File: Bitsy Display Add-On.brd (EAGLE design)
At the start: 35.6 x 17.8 mm, 13 parts, among them IC1 APX803, SW1 KMR2

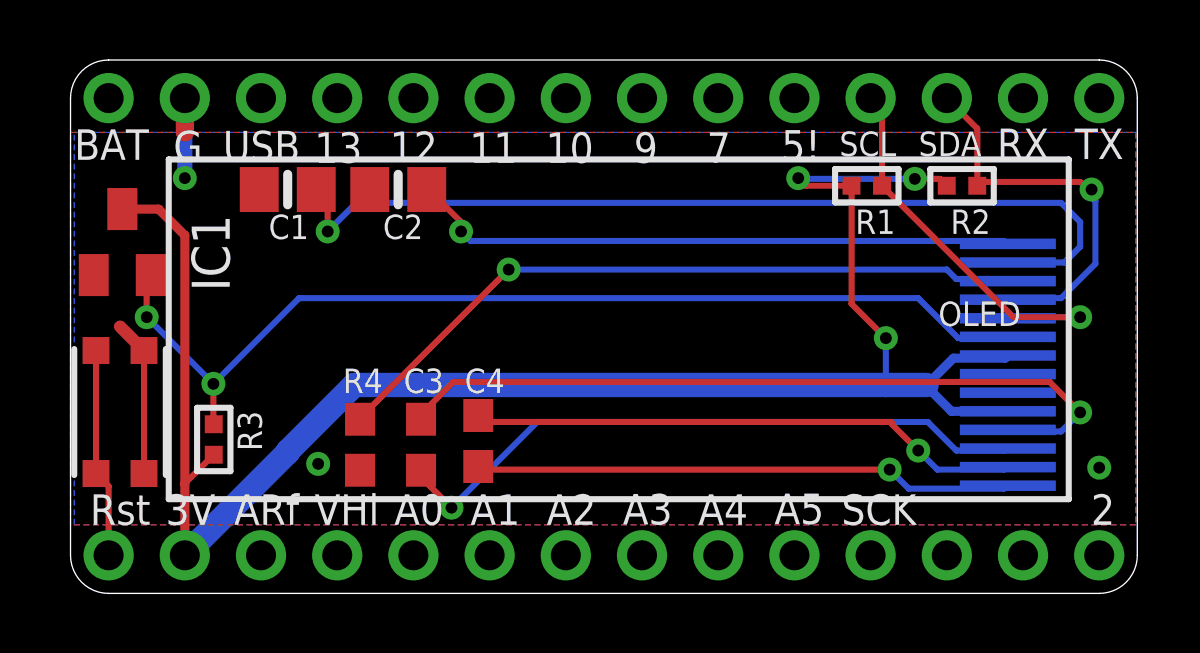
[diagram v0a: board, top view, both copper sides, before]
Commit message: PCB Redisgned
Resistors and Capacitors on bottom of board
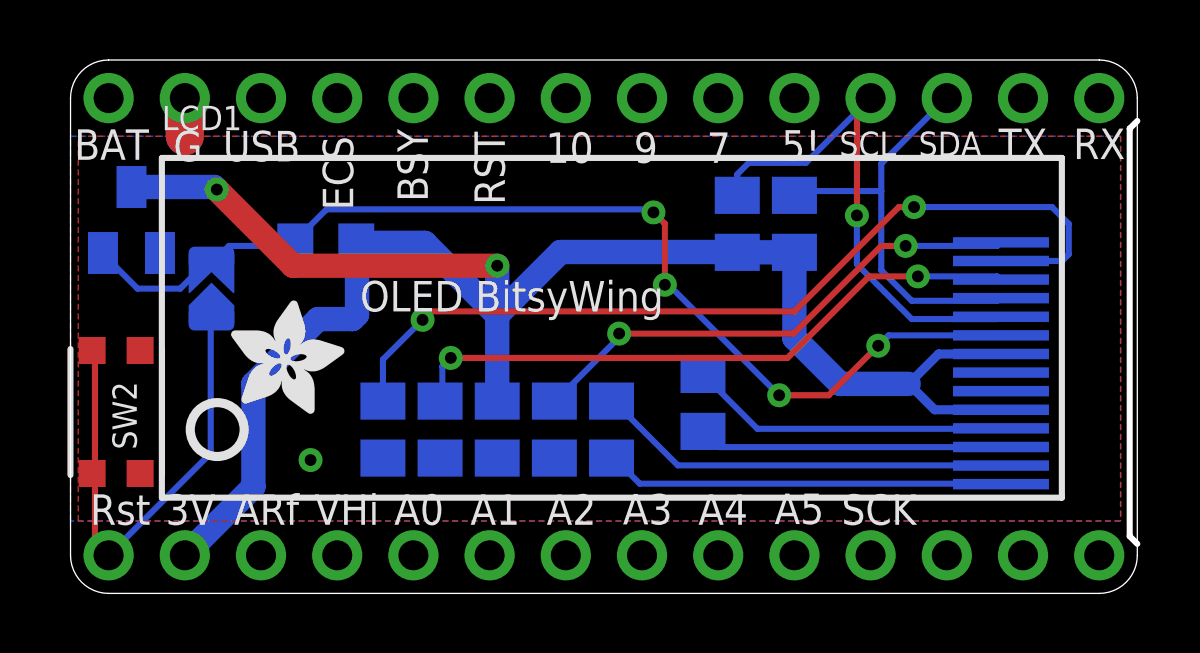
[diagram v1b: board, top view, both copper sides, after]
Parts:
- removed C3: 1uF, microbuilder:0603-NO
- removed IC1: APX803, adafruit:SOT23
- removed JP1: (no value), microbuilder:1X14_ROUND70
- removed OLED: OLED 128x32, microbuilder:UG-2832HSWEG02_WRAPUNDER
- removed R1: 2K, microbuilder:_0402
- removed SW1: KMR2, microbuilder:BTN_KMR2_4.6X2.8
- added C5, C6: 10uF, microbuilder:0805-NO
- added IC5: APX803, adafruit:SOT23
- added JP4: (no value), microbuilder:1X14_ROUND70
- added LCD1: OLED 128x32, microbuilder:UG-2832HSWEG02_WRAPUNDER
- added R7: 2.2K, microbuilder:0805-NO
- added SJ1: (no value), microbuilder:SOLDERJUMPER_ARROW_NOPASTE
- added SW2: KMR2, microbuilder:BTN_KMR2_4.6X2.8
- added U$6: (no value), microbuilder:PCBFEAT-REV-040
- added U$62: (no value), microbuilder:ADAFRUIT_3.5MM
- C1, C2: value 10uF -> 1uF
- C4: value 1uF -> 10uF; device microbuilder:0603-NO -> microbuilder:0805-NO
- R2: value 2K -> 10K; device microbuilder:_0402 -> microbuilder:_0805MP
- R3: value 10K -> 390K; device microbuilder:_0402 -> microbuilder:0805-NO
- R4: value 390K -> 2.2K; device microbuilder:0603-NO -> microbuilder:0805-NO
- moved R2 21.3 mm to (8.51, 11.7), flipped to the bottom
- moved R4 16.2 mm to (24.1, 12.3), flipped to the bottom, turned to 270 degrees
- moved JP2 15.2 mm to (17.8, 16.5), turned to 0 degrees
- moved C1 13.4 mm to (18.0, 5.46), flipped to the bottom, turned to 270 degrees
- moved C2 12.4 mm to (21.1, 6.35), flipped to the bottom, turned to 270 degrees
- moved R3 7.55 mm to (12.3, 5.46), flipped to the bottom, turned to 90 degrees
- moved C4 0.74 mm to (14.2, 5.46), flipped to the bottom, turned to 90 degrees
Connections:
- removed net VCC: C2.2, OLED.14
- removed net VCOMH: C1.2, OLED.13
- new net N$5: C6.2, LCD1.13
- new net N$6: C5.2, LCD1.14
- net !OLED_RST: now also IC5.2, LCD1.9, R2.1, SJ1.2; no longer IC1.2, OLED.9, R3.1
- net !RESET: now also JP4.14, SJ1.1, SW2.B, SW2.B'; no longer JP2.14, SW1.B, SW1.B'
- net 3.3V: now also C4.2, IC5.3, JP4.13, LCD1.5, LCD1.8, R4.2, R7.2; no longer IC1.3, JP2.13, OLED.5, OLED.8, R1.2, R3.2
- net A0: now also JP4.10; no longer JP2.10
- net A1: now also JP4.9; no longer JP2.9
- net A2: now also JP4.8; no longer JP2.8
- net A3: now also JP4.7; no longer JP2.7
- net A4: now also JP4.6; no longer JP2.6
- net A5: now also JP4.5; no longer JP2.5
- net AREF: now also JP4.12; no longer JP2.12
- net D10: now also JP2.7; no longer JP1.7
- net D11: now also JP2.6; no longer JP1.6
- net D12: now also JP2.5; no longer JP1.5
- net D13: now also JP2.4; no longer JP1.4
- net D2: now also JP4.1; no longer JP2.1
- net D5: now also JP2.10; no longer JP1.10
- net D7: now also JP2.9; no longer JP1.9
- net D9: now also JP2.8; no longer JP1.8
- net GND: now also C4.1, C5.1, C6.1, IC5.1, JP2.2, LCD1.7, R3.1, SW2.A, SW2.A'; no longer C1.1, C2.1, IC1.1, JP1.2, OLED.7, R4.1, SW1.A, SW1.A'
- net MISO: now also JP4.2; no longer JP2.2
- net MOSI: now also JP4.3; no longer JP2.3
- net N$1: now also C1.2, LCD1.1; no longer C4.2, OLED.1
- net N$2: now also C1.1, LCD1.2; no longer C4.1, OLED.2
- net N$3: now also C2.2, LCD1.3; no longer C3.2, OLED.3
- net N$4: now also C2.1, LCD1.4; no longer C3.1, OLED.4
- net N$7: now also LCD1.12, R3.2; no longer OLED.12, R4.2
- net RX: now also JP2.14; no longer JP1.13
- net SCK: now also JP4.4; no longer JP2.4
- net SCL: now also JP2.11, LCD1.10, R7.1; no longer JP1.11, OLED.10, R1.1
- net SDA: now also JP2.12, LCD1.11, R4.1; no longer JP1.12, OLED.11, R2.1
- net TX: now also JP2.13; no longer JP1.14
- net VBAT: now also JP2.1; no longer JP1.1
- net VBREF: now also LCD1.6; no longer OLED.6
- net VBUS: now also JP2.3; no longer JP1.3
- net VHI: now also JP4.11; no longer JP2.11
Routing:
- net VCOMH: track 30.7 -> 0.00 mm, vias 1 -> 0
- net N$5: track 0.00 -> 29.9 mm, vias 0 -> 2
- net VCC: track 20.3 -> 0.00 mm, vias 1 -> 0
- net N$6: track 0.00 -> 17.1 mm, vias 0 -> 2
- net N$4: track 25.7 -> 10.8 mm, vias 1 -> 0
- net N$3: track 21.8 -> 10.2 mm, vias 1 -> 0
- net !RESET: track 7.00 -> 16.4 mm
- net GND: track 9.04 -> 2.54 mm, vias 3 -> 1
- net N$1: track 18.0 -> 13.3 mm, vias 1 -> 0
- net N$2: track 18.5 -> 13.9 mm, vias 1 -> 0
- net SCL: track 13.9 -> 17.5 mm
- net N$7: track 23.8 -> 21.1 mm, vias 1 -> 2
- net !OLED_RST: track 34.2 -> 36.1 mm, vias 2 -> 4
- net SDA: track 13.2 -> 14.1 mm, vias 1 -> 0
- net 3.3V: track 61.9 -> 62.0 mm, vias 3 -> 2
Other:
- outline, holes or cut-outs redrawn
- board text added: "BSY"
- board text added: "ECS"
- board text added: "ERST"
- board text added: "ERX"
- board text added: "ETX"
- board text added: "GPIO0"
- board text added: "OLED BitsyWing"
- board text added: "RST"
- board text removed: "11"
- board text removed: "12"
- board text removed: "13"
- board text removed: "By"
- board text removed: "HEXTHAT"
- board text removed: "ItsyBitsy Display"
